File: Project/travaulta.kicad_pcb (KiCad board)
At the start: 4 copper layers, 209.7 x 76.4 mm, 106 parts, among them SW1 EC_SW, SW10 EC_SW, SW11 EC_SW, SW12 EC_SW, SW13 EC_SW, SW14 EC_SW, SW15 EC_SW, SW16 EC_SW, SW17 EC_SW, SW18 EC_SW, SW19 EC_SW, SW2 EC_SW, SW20 EC_SW, SW21 EC_SW, SW22 EC_SW, SW23 EC_SW, SW24 EC_SW, SW25 EC_SW, SW26 EC_SW, SW27 EC_SW, SW28 EC_SW, SW29 EC_SW, SW3 EC_SW, SW30 EC_SW, SW31 EC_SW, SW32 EC_SW, SW33 EC_SW, SW34 EC_SW, SW35 EC_SW, SW36 EC_SW, SW37 EC_SW, SW38 BOOT0, SW4 EC_SW, SW5 EC_SW, SW6 EC_SW, SW7 EC_SW, SW8 EC_SW, SW9 EC_SW, U1 STM32F401CBUx, U2 XC6206PxxxMR, U3 74HC4051, U4 74HC4051, U5 OPA350, Y1 8 MHz

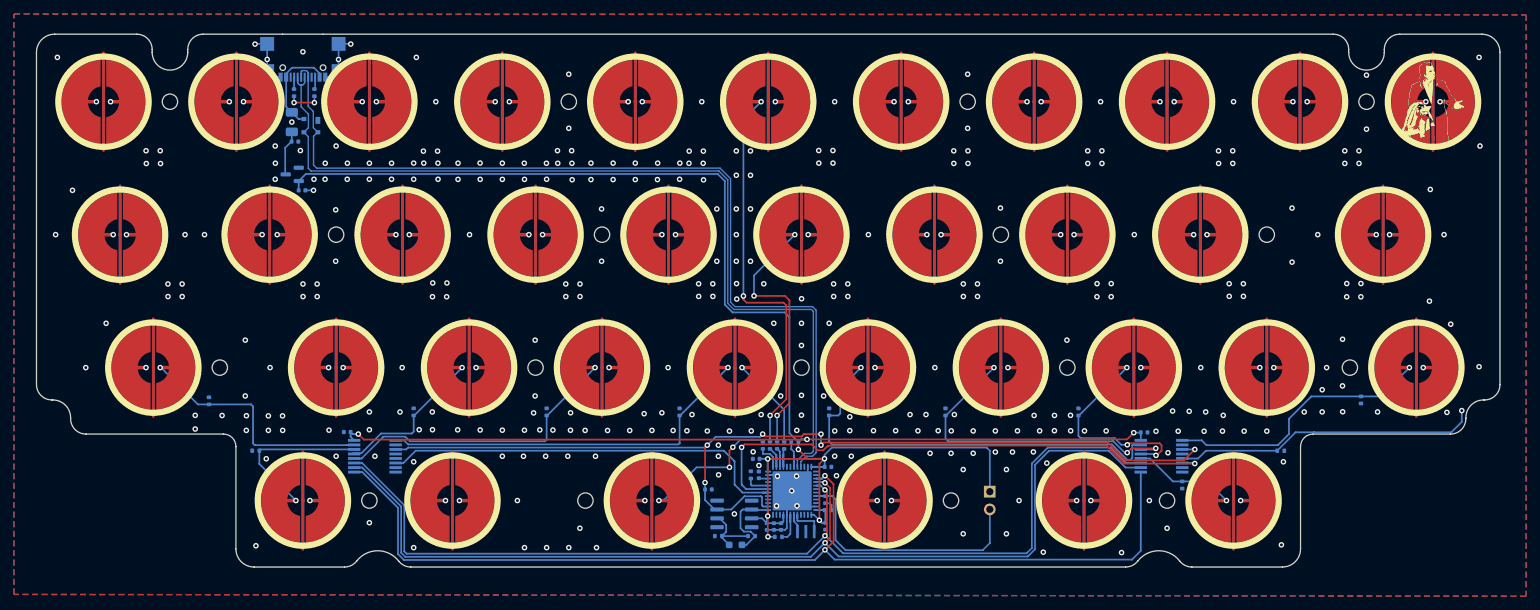
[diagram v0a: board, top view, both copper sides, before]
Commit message: add daughterboard header
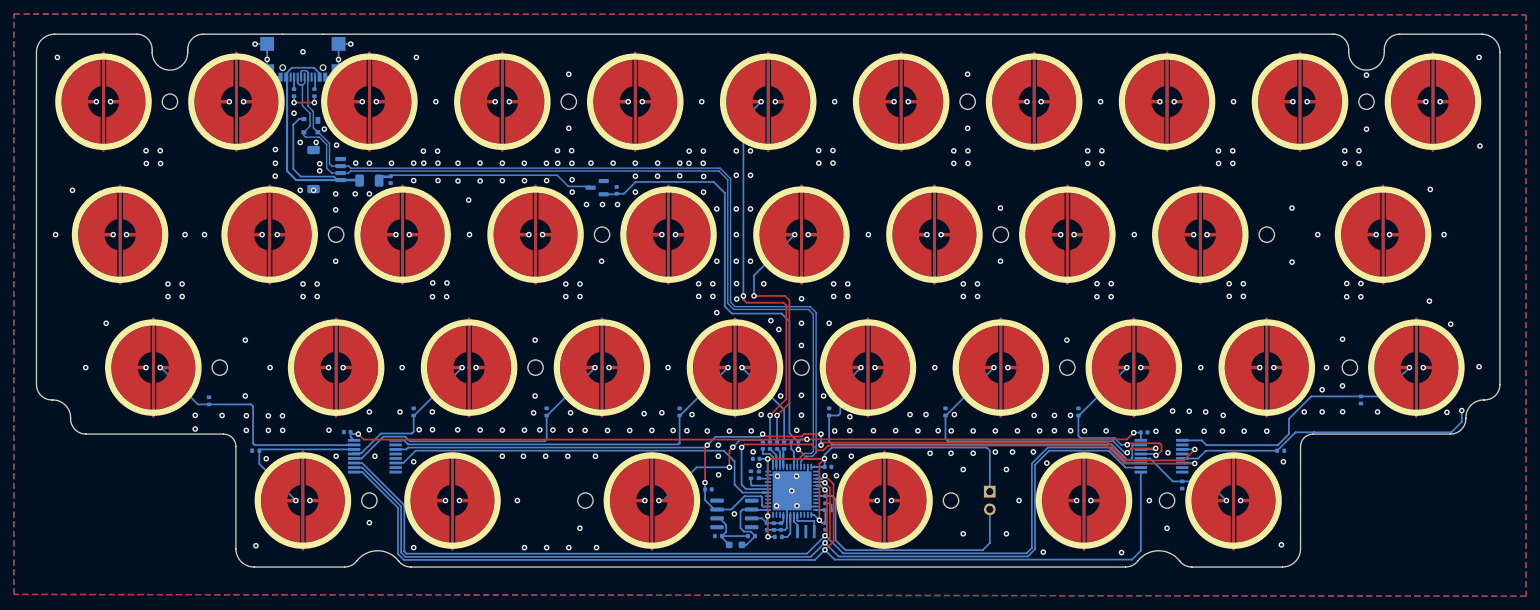
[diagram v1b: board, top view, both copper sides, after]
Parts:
- removed the G*** at (244.5, 57.1)
- removed the G*** at (69.8, 50.8)
- removed the G*** at (197.7, 72.8)
- removed the G*** at (98.4, 49.2)
- added J1: Conn_01x04_MountingPin, Connector_JST:JST_SH_SM04B-SRSS-TB_1x04-1MP_P1.00mm_Horizontal, B.Cu at (85.9, 66.9)
- moved C5 45.1 mm to (127.5, 69.8), turned to 90 degrees
- moved U2 43.7 mm to (124.7, 69.5)
- moved C4 14.8 mm to (95.1, 68.3), turned to -90 degrees
- moved F_USBC1 13.9 mm to (92.1, 68.5), turned to 0 degrees
- moved G*** 0.89 mm to (251.7, 76.2)
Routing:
- net VBAT: track 318.1 -> 271.6 mm
- net VCC: track 14.0 -> 47.1 mm
- net +5V: track 6.54 -> 31.3 mm
- net D+: track 131.0 -> 128.9 mm
- net GND: track 37.7 -> 36.5 mm, vias 326 -> 334
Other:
- board text added: "by Calvin0563 for mechvault's vault35 modified by mrninhvn"
- board text removed: "by Calvin0563 for mechvault's vault35"

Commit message: fix solder paste
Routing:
- net COL10: track 89.9 -> 88.9 mm
- net AMUX_SEL_2: track 148.7 -> 148.1 mm
- net AMUX_SEL_0: track 147.3 -> 146.8 mm
